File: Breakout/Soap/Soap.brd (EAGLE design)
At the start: 52 x 30.8 mm, 23 parts, among them U2 MCP73831

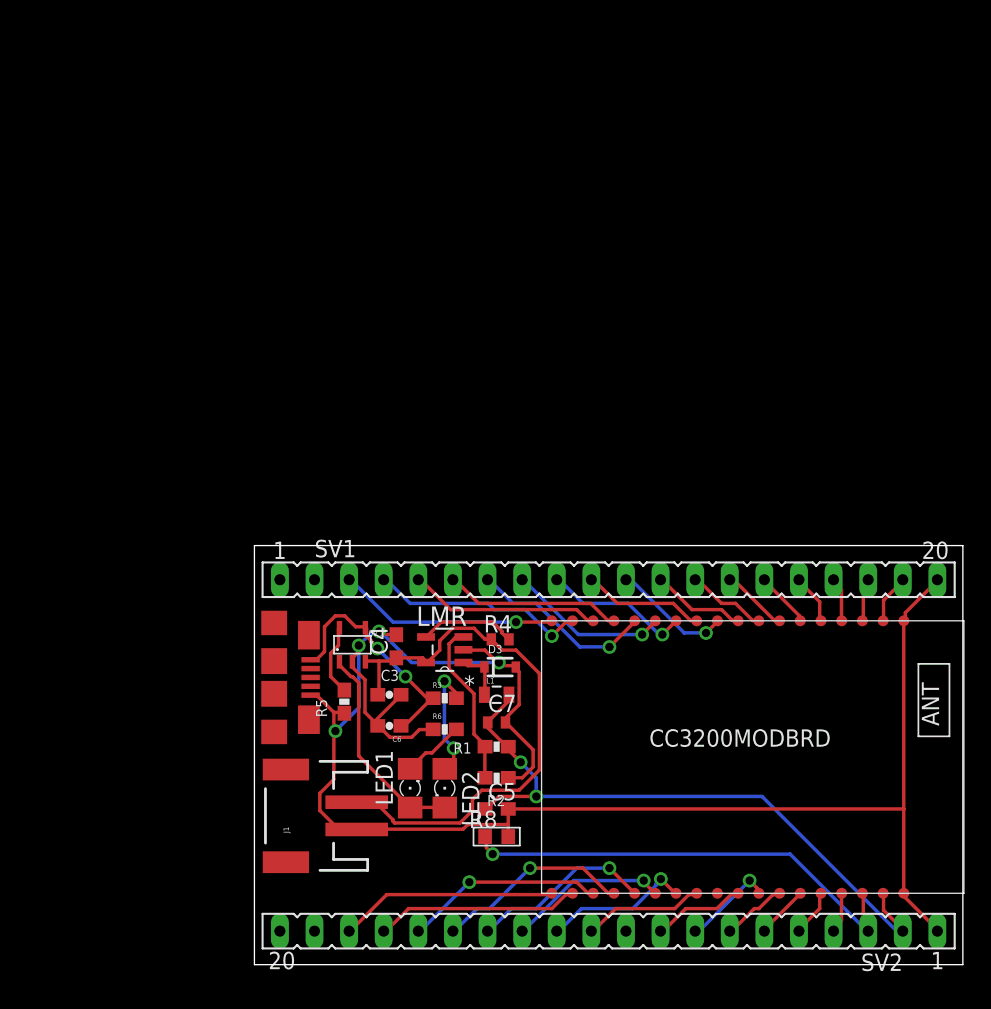
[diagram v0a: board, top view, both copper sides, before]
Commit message: switch charger
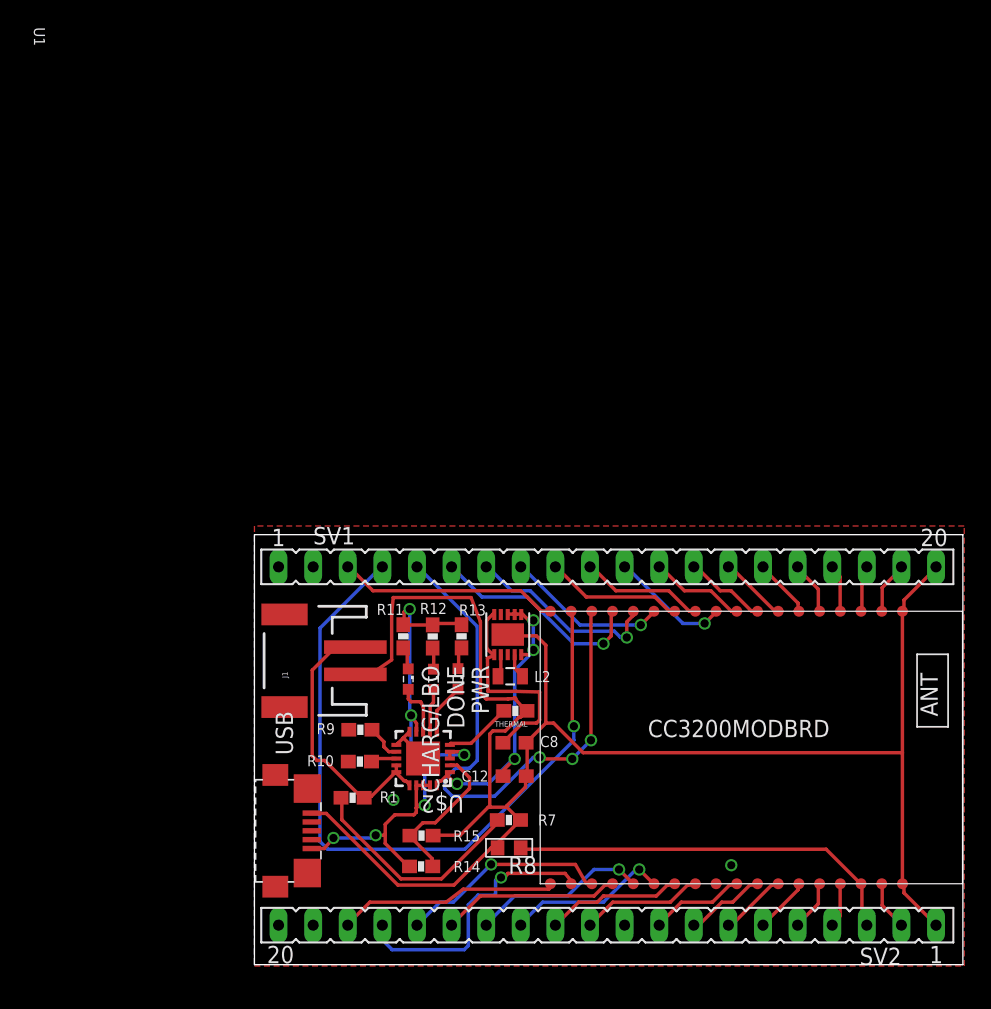
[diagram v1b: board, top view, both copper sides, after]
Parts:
- removed C3, C6: 4.7uF, SparkFun-Capacitors:0603-CAP
- removed C4, C5: 22uF, rcl:C0603
- removed C7: 0.1uF, adafruit:C0402
- removed D3: BAT20J, SparkFun-DiscreteSemi:SOD-323
- removed JP2: USB-RECEPTABLE-HIROSE-ZX62-AB-5PA(11), daspilker:HIROSE-ZX62-AB-5PA(11)
- removed L1: 2.2uH, Spark:0805
- removed LED1, LED2: (no value), eagle-ltspice:LED_1206
- removed LMR: MCP1824T-3302E/OT, Microchip_By_element14_Batch_1:SOT95P270X145-5N
- removed R2: 10K 1%, SparkFun-Resistors:0603-RES
- removed R3, R6: 470-Ohm, SparkFun-Resistors:0603-RES
- removed R4: 100K, adafruit:R0402
- removed R5: 2K, SparkFun-Resistors:0603-RES
- removed U2: MCP73831, BaseApp:5PIN_SOT23
- added C12, C8: 10uF, rcl:C0603
- added CHARG/LBO: ORANGE, led:SML0603
- added DONE: GREEN, led:SML0603
- added L2: 2.2uH, SparkFun-Passives:0805
- added PWR: RED, led:SML0603
- added R10: 100K, SparkFun-Passives:0603-RES
- added R11, R12, R13, R14, R15: 1K, SparkFun-Passives:0603-RES
- added R7: 100K, SparkFun-Resistors:0603-RES
- added R9: 2K, SparkFun-Passives:0603-RES
- added THERMAL: 10K, SparkFun-Passives:0603-RES
- added U$2: MCP73871-2CCI/ML, microchip-battery:QFN20-4X4
- added U1: TPS63001DRCT, TPS63001:SON50P300X300X100-11N
- added USB: MICRO-USB-ZX62R-B-5P, con-hirose:ZX62R-B-5P
- R1: value 45.2k 1% -> 470K
- moved J1 11.4 mm to (3.71, 22.3)
- moved R1 11.2 mm to (7.21, 12.3)
- moved R8 1.23 mm to (18.7, 8.57), turned to 180 degrees
- moved SV1 0.95 mm to (25.9, 29.2)
- moved U$1 0.71 mm to (36.5, 15.9)
- moved SV2 0.45 mm to (25.9, 2.90)
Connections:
- removed net FB: LMR.3, R1.1, R2.2
- removed net N$1: LED2.A, R3.2
- removed net N$2: LMR.4, R4.1
- removed net N$3: R5.2, U2.P$5
- removed net N$5: LED1.C, R6.2
- removed net STAT: LED1.A, LED2.C, U2.P$1
- removed net SW: D3.C, L1.1, LMR.1
- removed net VBAT: C3.1, C4.1, J1.2, LMR.5, R4.2, U2.P$3
- removed net VIN: C6.1, JP2.P$1, R3.1, U2.P$4
- new net +5V_USB: R11.2, R12.2, R13.2, R14.2, U$2.17, U$2.18, U$2.19, U$2.3, U$2.4, U$2.9, USB.1
- new net +BATT: J1.2, R1.2, U$2.14, U$2.15, U$2.16
- new net GPIO_05: R1.1, R7.2
- new net N$52: L2.1, U1.4
- new net N$53: L2.2, U1.2
- new net N$55: R9.2, U$2.12
- new net N$56: R10.2, U$2.13
- new net N$57: PWR.A, U$2.6
- new net N$58: DONE.A, U$2.7
- new net N$59: CHARG/LBO.A, U$2.8
- new net N$60: CHARG/LBO.C, R11.1
- new net N$61: DONE.C, R12.1
- new net N$62: PWR.C, R13.1
- new net N$63: R14.1, R15.2, U$2.2
- new net N$64: THERMAL.2, U$2.5
- new net OUT: C12.1, U$2.1, U$2.20, U1.5, U1.6, U1.7, U1.8
- new net VCC: C8.1, U1.1, U1.10
- net +3V3: no longer C5.1, C7.1, L1.2, R1.2
- net GND: now also C12.2, C8.2, R10.1, R15.1, R7.1, R9.1, THERMAL.1, U$2.10, U$2.11, U$2.21, U1.11, U1.3, U1.9, USB.5; no longer C3.2, C4.2, C5.2, C6.2, C7.2, D3.A, JP2.P$5, LMR.2, R2.1, R5.1, R6.1, U2.P$2
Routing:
- net +3V3: track 48.3 -> 3.62 mm, vias 2 -> 0
- net +5V_USB: track 0.00 -> 42.9 mm, vias 0 -> 6
- net VBAT: track 41.7 -> 0.00 mm
- net N$15: track 16.2 -> 53.9 mm
- net N$16: track 14.2 -> 42.1 mm, vias 0 -> 3
- net OUT: track 0.00 -> 22.9 mm, vias 0 -> 4
- net +BATT: track 0.00 -> 20.3 mm
- net VIN: track 17.6 -> 0.00 mm, vias 2 -> 0
- net GPIO_05: track 0.00 -> 16.8 mm
- net VCC: track 0.00 -> 15.8 mm
- net STAT: track 15.5 -> 0.00 mm
- net FB: track 12.2 -> 0.00 mm
- net N$63: track 0.00 -> 11.4 mm
- net N$1: track 8.62 -> 0.00 mm, vias 2 -> 0
- net N$2: track 7.12 -> 0.00 mm
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- added copper zone on layer 1, net GND
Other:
- board size 52 x 30.8 mm -> 52 x 31.6 mm
